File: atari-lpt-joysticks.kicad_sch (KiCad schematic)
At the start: 4 parts, among them J1 DB25_Male, J2 Barrel_Jack_Switch

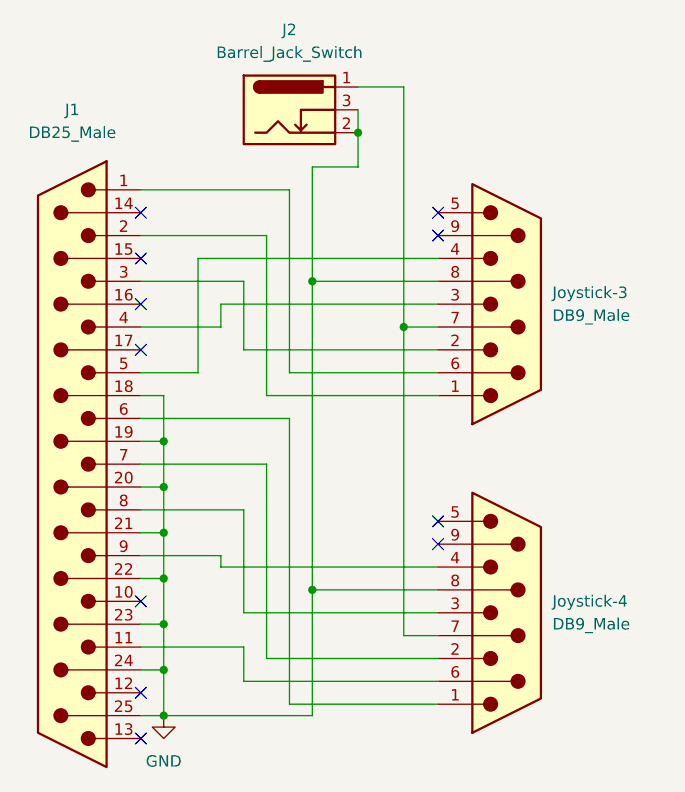
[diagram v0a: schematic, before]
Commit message: swap joystick 3 and 4
hardware description are not correct :
 * http://atari4ever.free.fr/hardware/zip/4joy_ada.zip
 * https://www.atari-forum.com/viewtopic.php?p=318615#p318615

Gauntlet 2 and Leatherneck game use this pinout

Discussion : https://github.com/hatari/hatari/pull/22
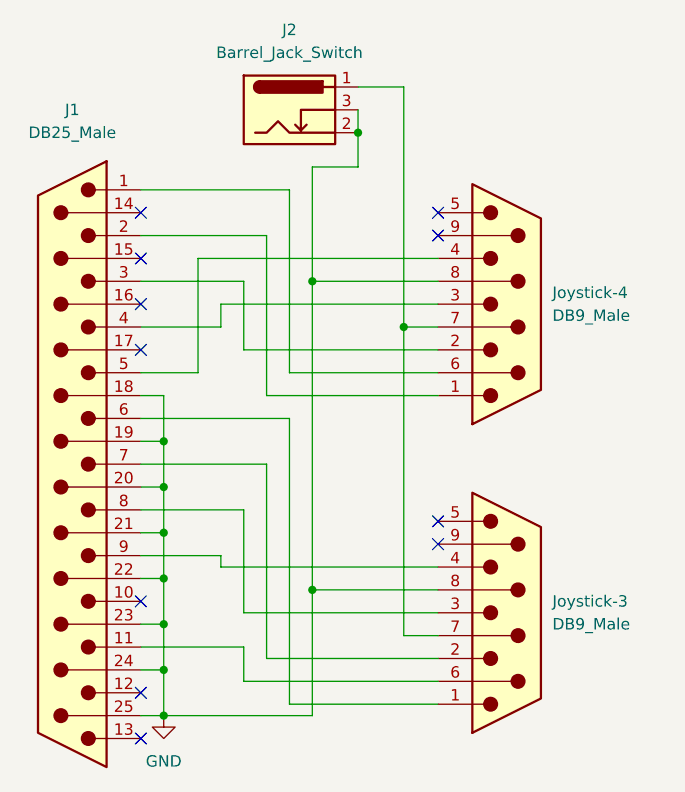
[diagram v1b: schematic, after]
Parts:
- renumbered Joystick-4 to Joystick-3, Joystick-3 to Joystick-4
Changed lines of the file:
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@@
   (symbol (lib_id "Connector:DB9_Male") (at 167.64 80.01 0) (unit 1)
     (in_bom yes) (on_board yes) (fields_autoplaced)
-    (property "Reference" "Joystick-3" (id 0) (at 172.72 78.7399 0)
+    (property "Reference" "Joystick-4" (id 0) (at 172.72 78.7399 0)
       (effects (font (size 1.27 1.27)) (justify left))
     )
@@
   (symbol (lib_id "Connector:DB9_Male") (at 167.64 114.3 0) (unit 1)
     (in_bom yes) (on_board yes) (fields_autoplaced)
-    (property "Reference" "Joystick-4" (id 0) (at 172.72 113.0299 0)
+    (property "Reference" "Joystick-3" (id 0) (at 172.72 113.0299 0)
       (effects (font (size 1.27 1.27)) (justify left))
     )
@@
       (reference "J2") (unit 1) (value "Barrel_Jack_Switch") (footprint "Connector_BarrelJack:BarrelJack_GCT_DCJ200-10-A_Horizontal")
     )
-    (path "/dfc60009-ef84-463c-81a8-51259230fe13"
+    (path "/eb50cb5e-4d03-48bb-9b03-0a49ba919bcd"
       (reference "Joystick-3") (unit 1) (value "DB9_Male") (footprint "Connector_Dsub:DSUB-9_Male_EdgeMount_P2.77mm")
     )
-    (path "/eb50cb5e-4d03-48bb-9b03-0a49ba919bcd"
+    (path "/dfc60009-ef84-463c-81a8-51259230fe13"
       (reference "Joystick-4") (unit 1) (value "DB9_Male") (footprint "Connector_Dsub:DSUB-9_Male_EdgeMount_P2.77mm")
     )
